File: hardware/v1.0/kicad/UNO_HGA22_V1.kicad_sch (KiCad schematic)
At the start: 59 parts, among them J1 Power, J3 Analog, J4 Digital/PWM, Q1 BSS138, U1 LM321LV, U2 LM321LV, U3 LP5907MFX-3.3, U4 LP5907MFX-4.5

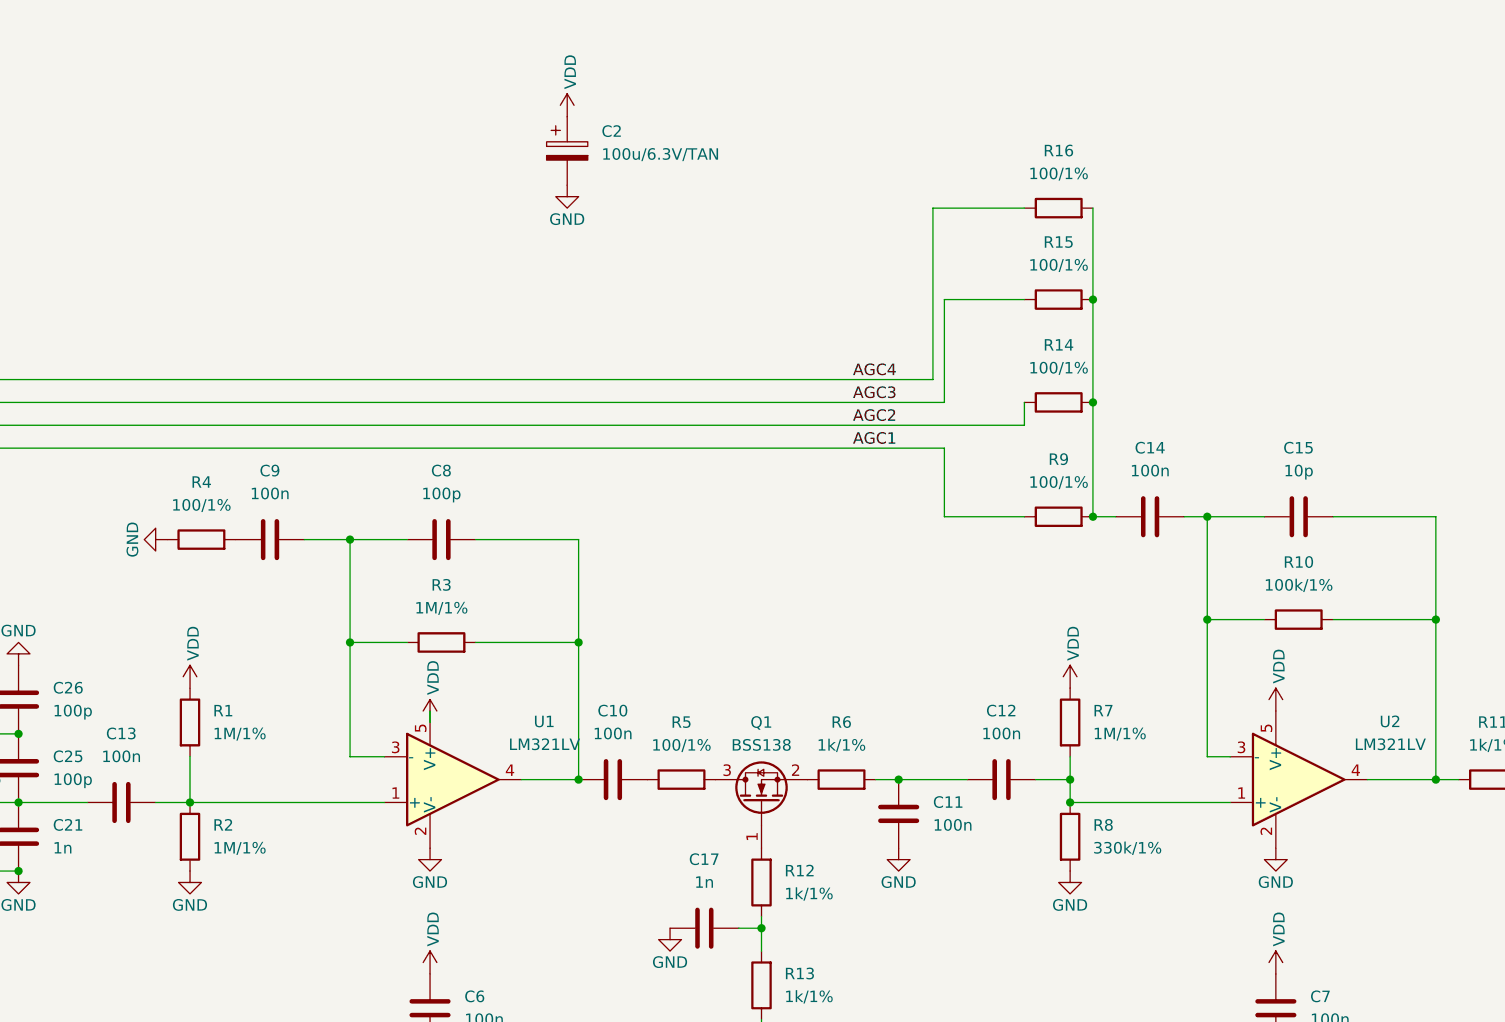
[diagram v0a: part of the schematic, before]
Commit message: Update HW Documentation. Fixing Schematic and PCB Silkscreen. Added generated Interactive BOM.
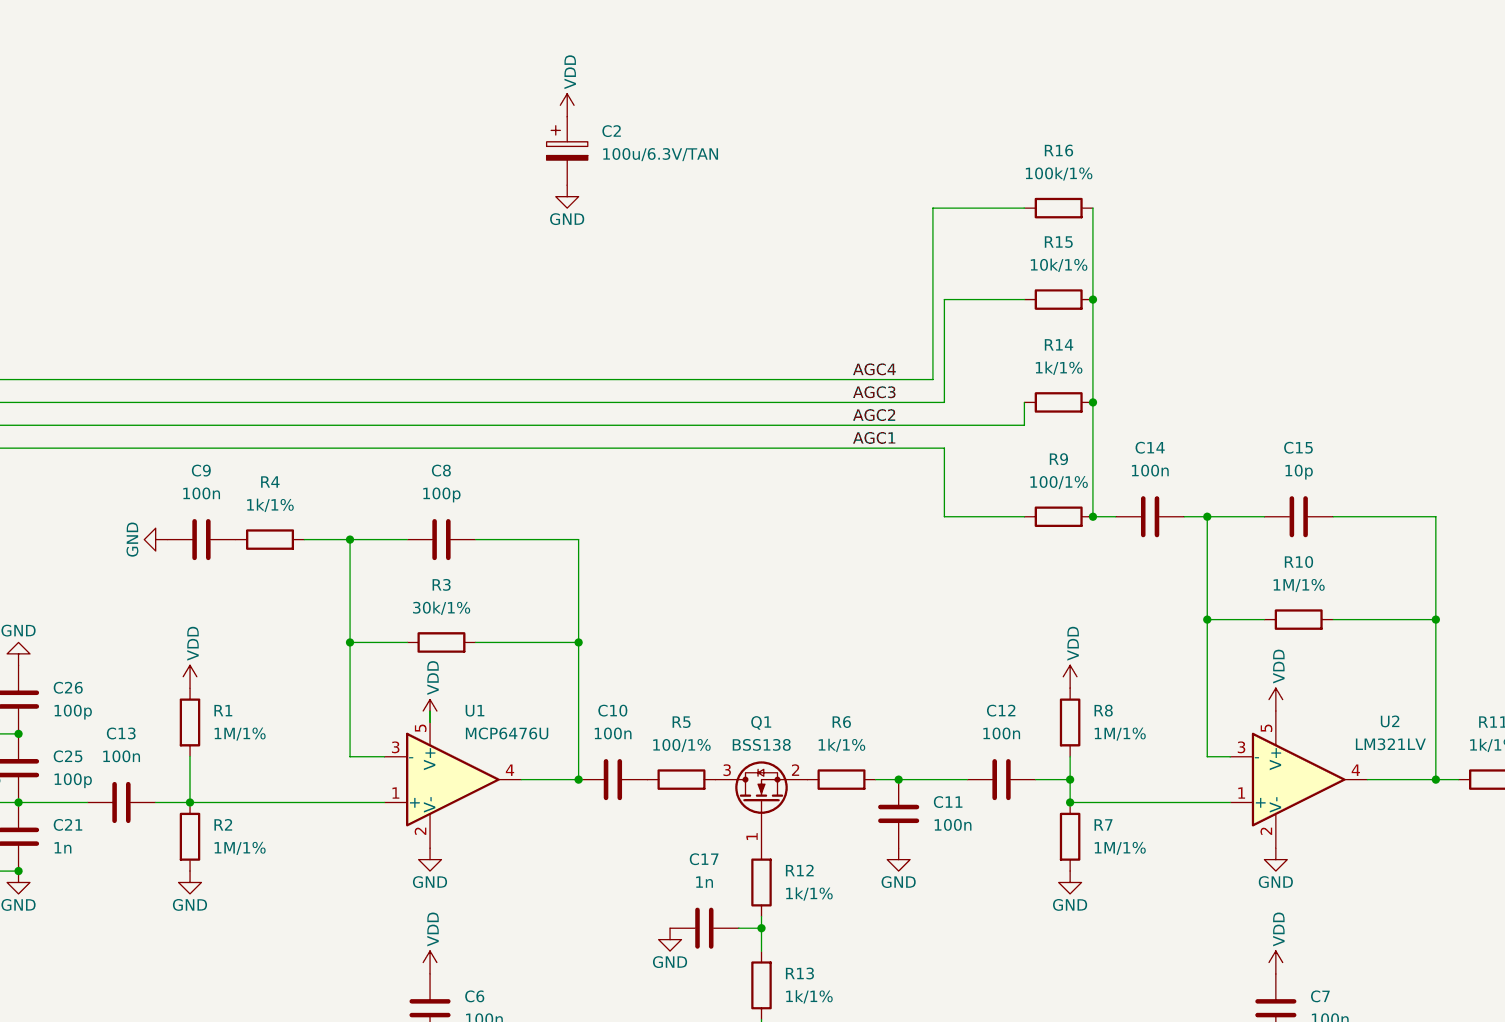
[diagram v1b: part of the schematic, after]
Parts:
- R10: value 100k/1% -> 1M/1%
- R14, R4: value 100/1% -> 1k/1%
- R15: value 100/1% -> 10k/1%
- R16: value 100/1% -> 100k/1%
- R3: value 1M/1% -> 30k/1%
- R7: renamed from R8; value 330k/1% -> 1M/1%
- U1: value LM321LV -> MCP6476U
- renumbered R7 to R8
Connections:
- net GND: now also C9.1; no longer R4.1
- net at R4.2: now also C8.1, R3.1, U1.3 (-); no longer C9.1
- new net: C9.2, R4.1
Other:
- moved on the sheet: C9, R4
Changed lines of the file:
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@@
 	(title_block
 		(title "UNO HGA22 Receiver")
-		(date "2025-12-19")
-		(rev "V1")
+		(date "2026-03-13")
+		(rev "V1.1")
 		(company "OSHW")
 	)
@@
 	(symbol
 		(lib_id "Device:R")
-		(at 102.87 77.47 90)
+		(at 110.49 77.47 90)
 		(unit 1)
 		(exclude_from_sim no)
@@
 		(fields_autoplaced yes)
 		(property "Reference" "R4"
-			(at 102.87 71.12 90)
+			(at 110.49 71.12 90)
 			(effects
 				(font
@@
 			)
 		)
-		(property "Value" "100/1%"
-			(at 102.87 73.66 90)
+		(property "Value" "1k/1%"
+			(at 110.49 73.66 90)
 			(effects
 				(font
@@
 		)
 		(property "Footprint" "Resistor_SMD:R_0805_2012Metric_Pad1.20x1.40mm_HandSolder"
-			(at 102.87 79.248 90)
+			(at 110.49 79.248 90)
 			(effects
 				(font
@@
 		)
 		(property "Datasheet" "~"
-			(at 102.87 77.47 0)
+			(at 110.49 77.47 0)
 			(effects
 				(font
@@
 		)
 		(property "Description" "Resistor"
-			(at 102.87 77.47 0)
+			(at 110.49 77.47 0)
 			(effects
 				(font
@@
 			)
 		)
-		(property "Value" "100/1%"
+		(property "Value" "10k/1%"
 			(at 198.12 46.99 90)
 			(effects
@@
 		(dnp no)
 		(fields_autoplaced yes)
-		(property "Reference" "R8"
+		(property "Reference" "R7"
 			(at 201.93 109.2199 0)
 			(effects
@@
 			)
 		)
-		(property "Value" "330k/1%"
+		(property "Value" "1M/1%"
 			(at 201.93 111.7599 0)
 			(effects
@@
 			(project "STM32_HGA22_V1"
 				(path "/e63e39d7-6ac0-4ffd-8aa3-1841a4541b55"
-					(reference "R8")
+					(reference "R7")
 					(unit 1)
 				)
@@
 			)
 		)
-		(property "Value" "100/1%"
+		(property "Value" "100k/1%"
 			(at 198.12 36.83 90)
 			(effects
@@
 	(symbol
 		(lib_id "Device:C")
-		(at 110.49 77.47 90)
+		(at 102.87 77.47 90)
 		(unit 1)
 		(exclude_from_sim no)
@@
 		(fields_autoplaced yes)
 		(property "Reference" "C9"
-			(at 110.49 69.85 90)
+			(at 102.87 69.85 90)
 			(effects
 				(font
@@
 		)
 		(property "Value" "100n"
-			(at 110.49 72.39 90)
+			(at 102.87 72.39 90)
 			(effects
 				(font
@@
 		)
 		(property "Footprint" "Capacitor_SMD:C_0805_2012Metric_Pad1.18x1.45mm_HandSolder"
-			(at 114.3 76.5048 0)
+			(at 106.68 76.5048 0)
 			(effects
 				(font
@@
 		)
 		(property "Datasheet" "~"
-			(at 110.49 77.47 0)
+			(at 102.87 77.47 0)
 			(effects
 				(font
@@
 		)
 		(property "Description" "Unpolarized capacitor"
-			(at 110.49 77.47 0)
+			(at 102.87 77.47 0)
 			(effects
 				(font
@@
 			)
 		)
-		(property "Value" "1M/1%"
+		(property "Value" "30k/1%"
 			(at 129.54 85.09 90)
 			(effects
@@
 		(on_board yes)
 		(dnp no)
-		(fields_autoplaced yes)
 		(property "Reference" "U1"
-			(at 140.97 97.7198 0)
+			(at 132.08 96.52 0)
 			(effects
 				(font
 					(size 1.27 1.27)
 				)
+				(justify left)
 			)
 		)
-		(property "Value" "LM321LV"
-			(at 140.97 100.2598 0)
+		(property "Value" "MCP6476U"
+			(at 132.08 99.06 0)
 			(effects
 				(font
 					(size 1.27 1.27)
 				)
+				(justify left)
 			)
 		)
@@
 			)
 		)
-		(property "Datasheet" "http://www.ti.com/lit/ds/symlink/lm321.pdf"
+		(property "Datasheet" "https://ww1.microchip.com/downloads/aemDocuments/documents/APID/ProductDocuments/DataSheets/MCP6476-6R-6U-7-9-Data-Sheet-20006419B.pdf"
 			(at 130.81 104.14 0)
 			(effects
@@
 		(dnp no)
 		(fields_autoplaced yes)
-		(property "Reference" "R7"
+		(property "Reference" "R8"
 			(at 201.93 96.5199 0)
 			(effects
@@
 			(project "STM32_HGA22_V1"
 				(path "/e63e39d7-6ac0-4ffd-8aa3-1841a4541b55"
-					(reference "R7")
+					(reference "R8")
 					(unit 1)
 				)
@@
 			)
 		)
-		(property "Value" "100k/1%"
+		(property "Value" "1M/1%"
 			(at 224.79 82.55 90)
 			(effects
@@
 			)
 		)
-		(property "Value" "100/1%"
+		(property "Value" "1k/1%"
 			(at 198.12 58.42 90)
 			(effects
